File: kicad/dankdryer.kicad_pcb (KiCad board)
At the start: 2 copper layers, 100 x 75 mm, 53 parts, among them J10 HeaderX4, J13 barreljack, J2 to microboard, J3 to baseboard, J4 ScrewX2, J5 ScrewX4, J6 LCD, J7 HeaderX4, J8 ScrewX2, J9 UART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

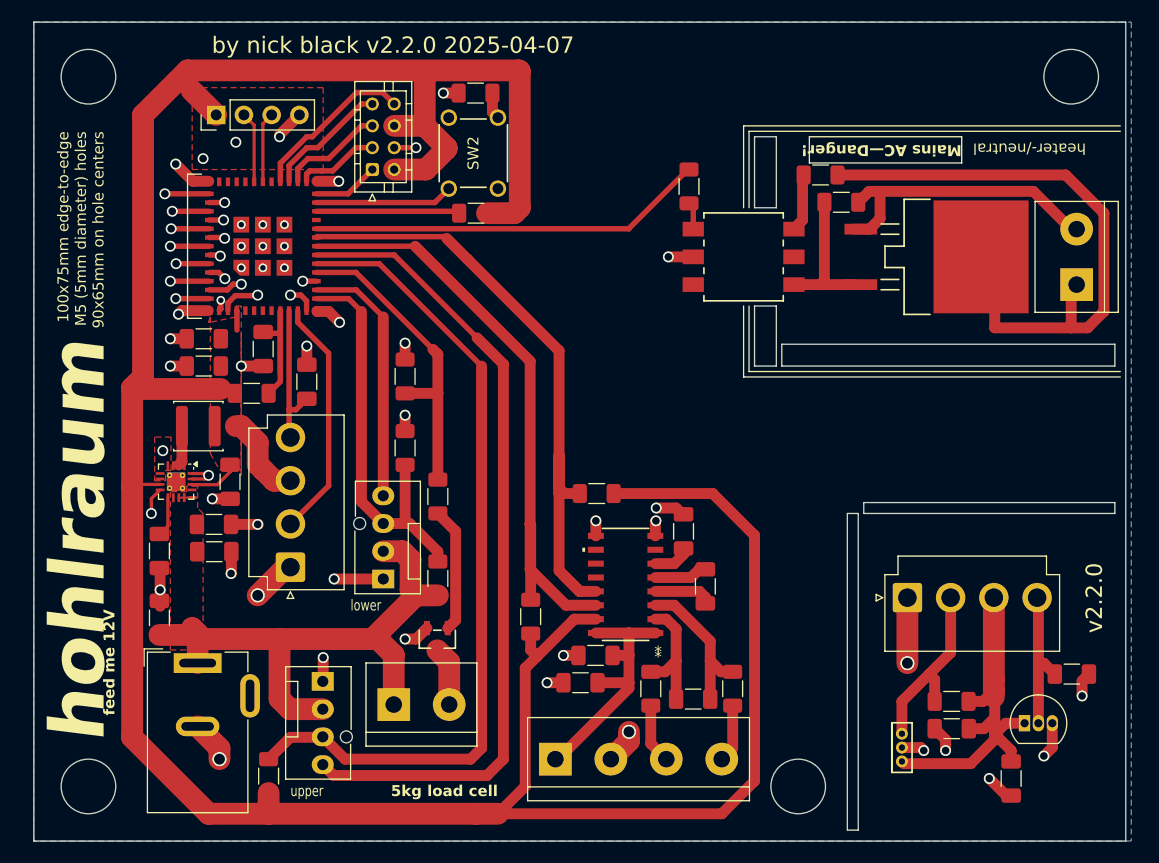
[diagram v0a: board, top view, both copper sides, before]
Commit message: [pcb] eliminate voltage divider before ltach closes #112
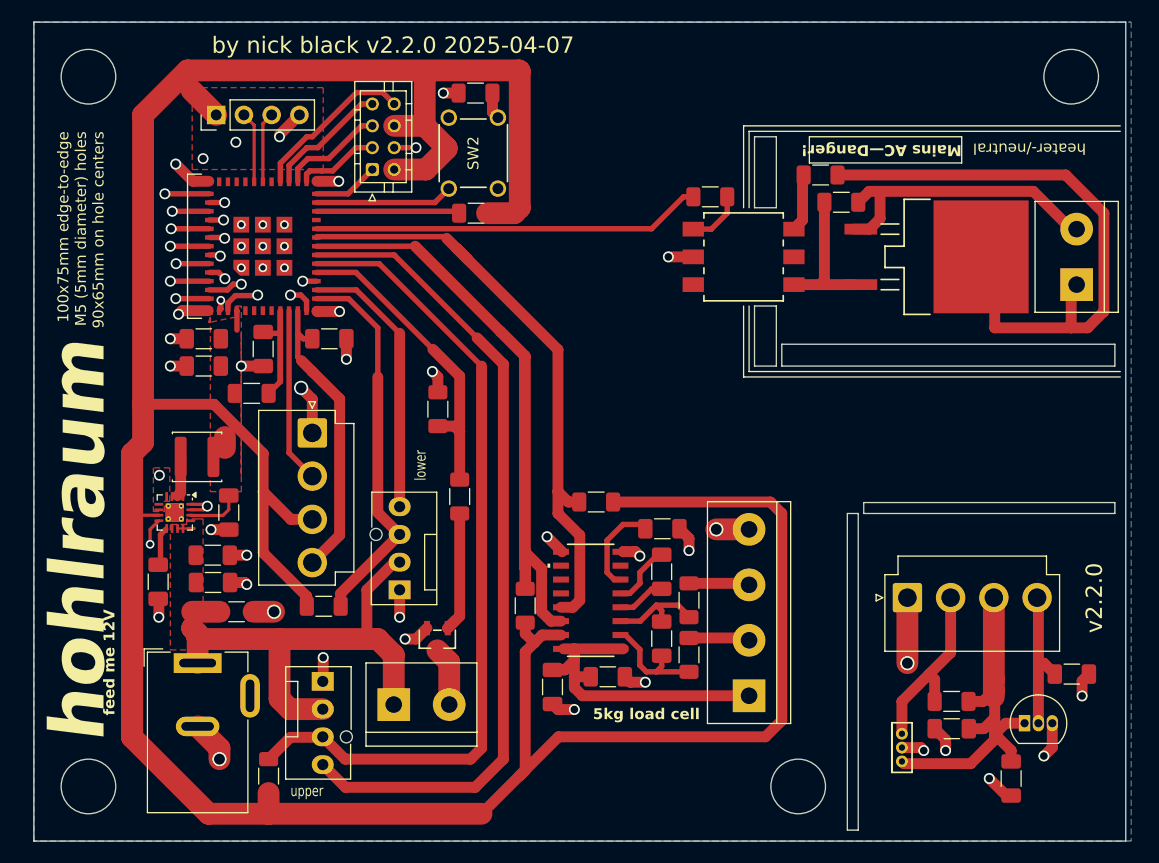
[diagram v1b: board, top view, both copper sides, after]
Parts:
- removed R18: 2.2k, Resistor_SMD:R_1206_3216Metric_Pad1.30x1.75mm_HandSolder
- R5: value 6.8k -> 680
- moved J5 18.7 mm to (115.5, 111.7), turned to 90 degrees
- moved J2 12.5 mm to (75.5, 87.6), turned to -90 degrees
- moved R5 10.8 mm to (76.5, 103.5), turned to 0 degrees
- moved R11 9.03 mm to (110.0, 103.0), turned to -90 degrees
- moved C14 7.08 mm to (68.6, 104.0), turned to 0 degrees
- moved C9 6.24 mm to (107.5, 106.5), turned to 90 degrees
- moved R10 4.68 mm to (110.0, 108.0), turned to -90 degrees
- moved C20 4.44 mm to (77.1, 79.0), turned to 0 degrees
- moved R7 4.24 mm to (87.0, 85.5)
- moved C11 4.22 mm to (107.5, 100.3)
- moved U3 3.51 mm to (101.0, 103.0)
- moved C21 2.82 mm to (67.9, 94.9)
- moved C2 2.82 mm to (66.4, 101.3)
- moved C1 2.82 mm to (66.4, 98.8)
- moved C7 2.82 mm to (61.4, 101.3)
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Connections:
- J5 pad 2: GND -> A-
- J5 pad 3: A- -> A+
- J5 pad 4: A+ -> GND
- R5 pad 1: +12V -> +3.3V
- U6 pad 10: /Hall -> /Therm
- U6 pad 9: /Therm -> /Hall
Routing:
- net +3.3V: track 281.1 -> 319.5 mm
- net /SDA: track 57.3 -> 77.4 mm
- net /Therm: track 13.5 -> 28.6 mm
- net +12V: track 56.3 -> 49.6 mm
- net /Hall: track 22.2 -> 16.0 mm
- net /SCL: track 64.5 -> 58.7 mm
- net Net-(U3-VIN1P): track 14.2 -> 9.00 mm
- net E+: track 24.1 -> 29.2 mm
- net Net-(U3-VBG): track 3.48 -> 8.14 mm
- net Net-(OC1-A): track 2.03 -> 5.21 mm
- net GND: track 134.4 -> 132.4 mm
- net /LTach: track 37.2 -> 35.3 mm
- net Net-(U3-VIN1N): track 11.4 -> 9.75 mm
- net /LPWM: track 23.5 -> 25.2 mm
- net /UPWM: track 75.0 -> 75.9 mm
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
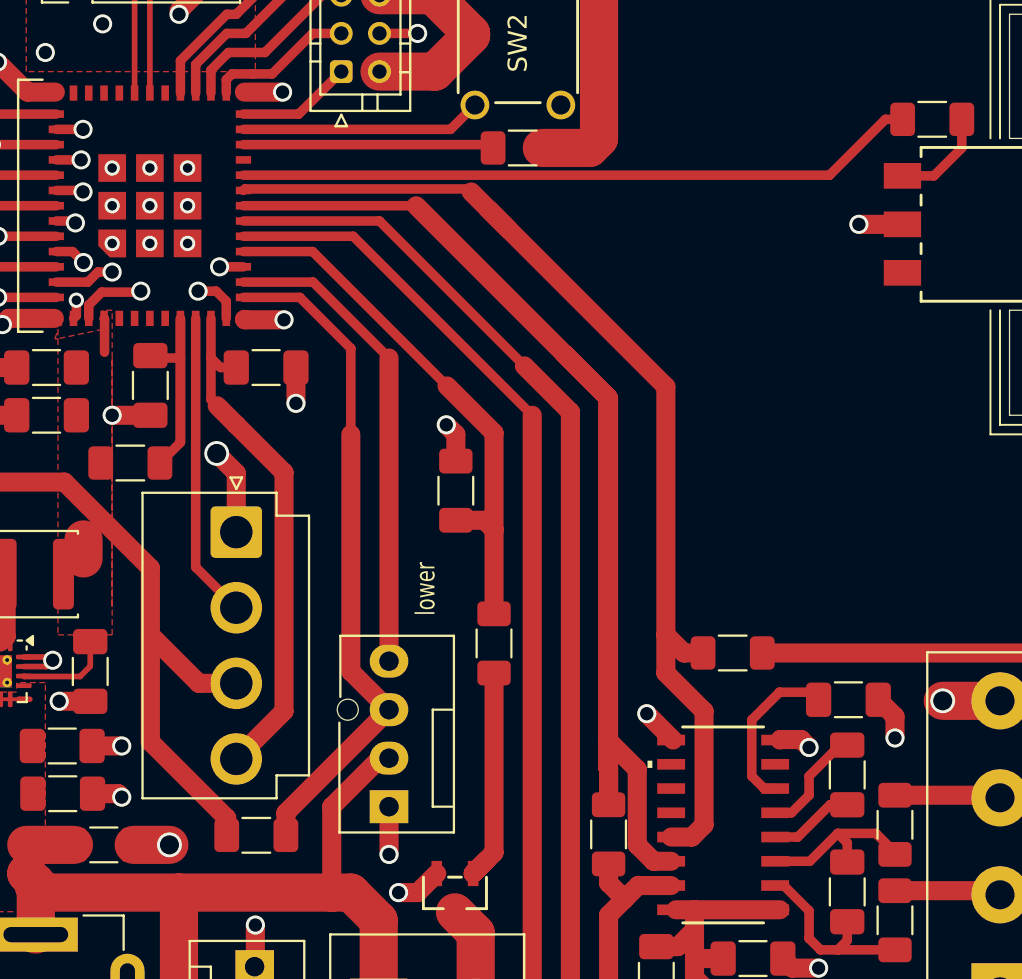
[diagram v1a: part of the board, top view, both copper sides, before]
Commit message: [pcb] reorient load cell hookup
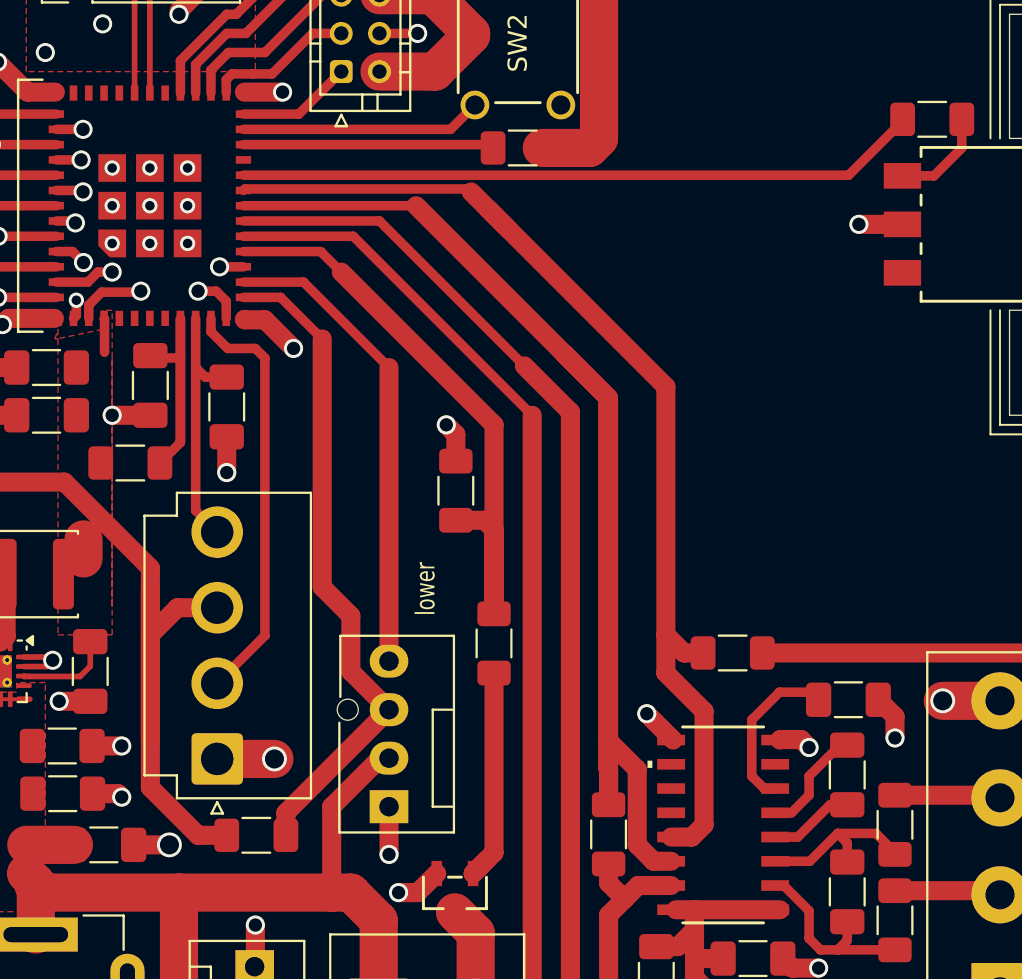
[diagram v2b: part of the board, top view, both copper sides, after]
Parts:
- moved J2 11.9 mm to (74.5, 99.5), turned to 90 degrees
- moved C20 2.92 mm to (75.0, 81.1), turned to -90 degrees
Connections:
- U6 pad 10: /Therm -> /Hall
- U6 pad 9: /Hall -> /Therm
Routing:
- net /Therm: track 28.6 -> 13.5 mm
- net /Motor: track 28.7 -> 38.5 mm
- net +3.3V: track 319.5 -> 327.0 mm
- net /Hall: track 16.0 -> 22.2 mm
- net /LTach: track 35.3 -> 34.7 mm

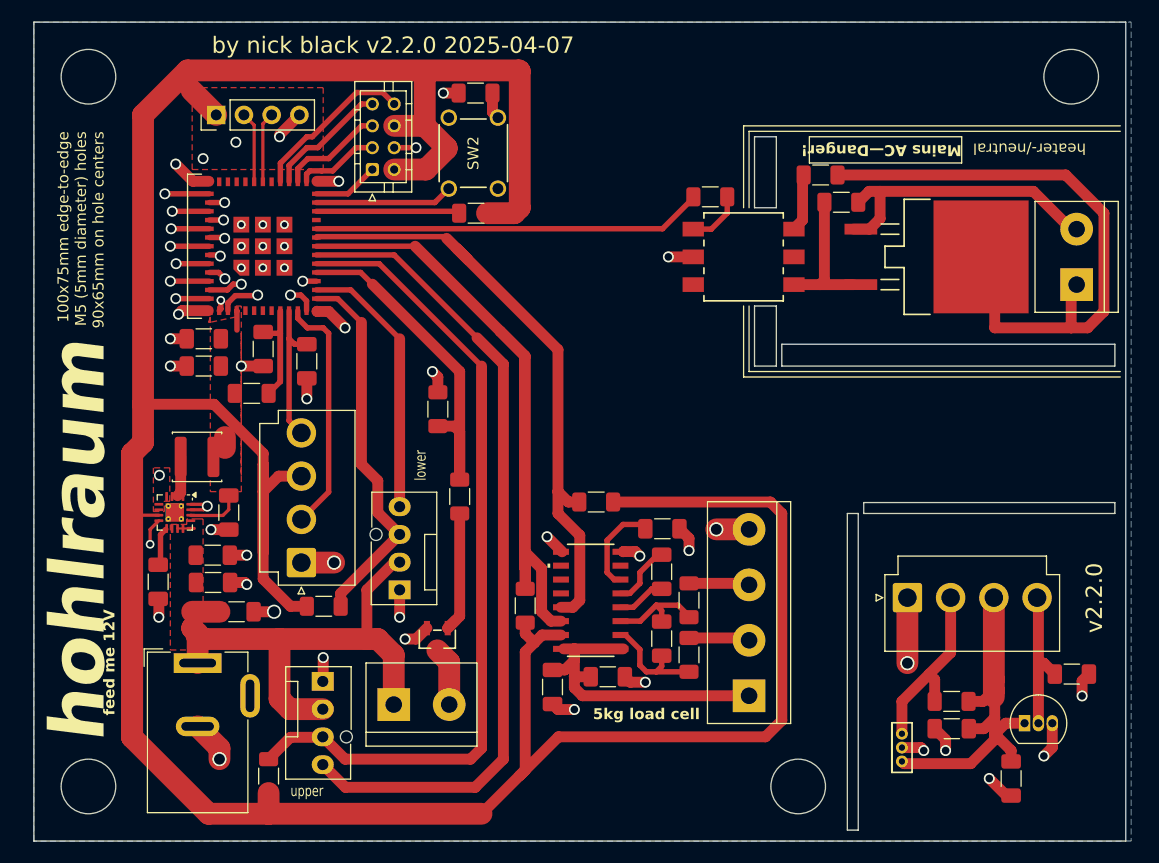
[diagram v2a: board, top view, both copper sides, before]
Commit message: [pcb] label load cell hookups
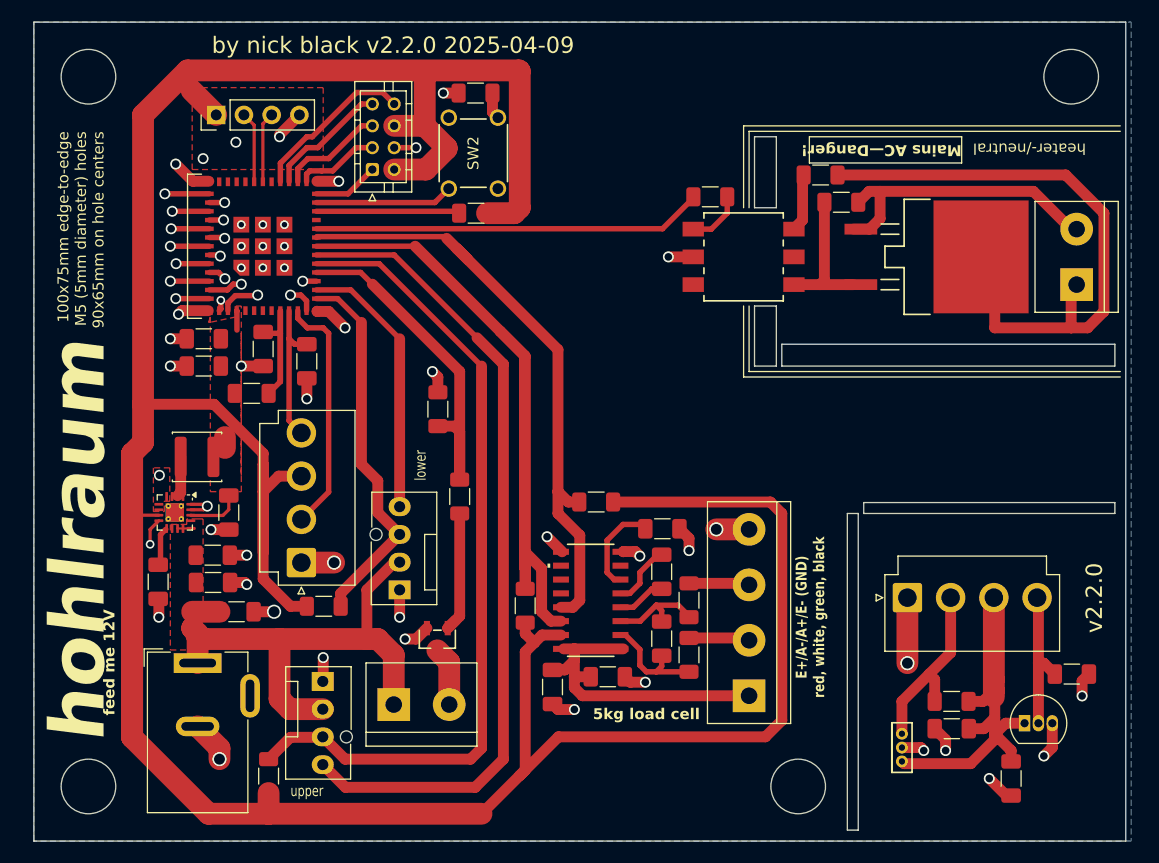
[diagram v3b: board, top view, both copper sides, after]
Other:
- board text added: "E+/A-/A+/E- (GND) red, white, green, black"
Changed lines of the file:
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@@
 	(title_block
 		(title "hohlraum")
-		(date "2025-04-07")
+		(date "2025-04-09")
 		(rev "v2.2.0")
 		(company "dirty south supercomputing")
@@
 		)
 	)
+	(gr_text "E+/A-/A+/E- (GND)\nred, white, green, black"
+		(at 122.5 104.5 90)
+		(layer "F.SilkS")
+		(effects
+			(font
+				(size 1 0.8)
+				(thickness 0.15)
+				(bold yes)
+			)
+			(justify bottom)
+		)
+	)

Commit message: kicad/scad v2.2.2
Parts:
- moved Q1 8.64 mm to (138.0, 119.0), turned to 180 degrees
- moved R8 5.50 mm to (95.0, 109.0)
- moved C8 3.50 mm to (104.1, 96.4), turned to 180 degrees
- moved C11 3.15 mm to (109.0, 97.6)
- moved C19 3.12 mm to (142.1, 117.5), turned to 180 degrees
- moved C12 2.26 mm to (104.6, 111.0)
- moved C5 2.00 mm to (99.5, 111.0)
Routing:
- net /SDA: track 77.4 -> 54.3 mm
- net +3.3Vmicro: track 35.9 -> 28.9 mm
- net /Microboard/HallMicro: track 17.0 -> 22.2 mm
- net GND: track 131.9 -> 127.8 mm
- net Net-(U3-VIN2P): track 5.46 -> 9.23 mm
- net Net-(U3-VIN2N): track 4.48 -> 6.97 mm
- net E+: track 29.2 -> 27.3 mm
- net Net-(U3-VBG): track 8.14 -> 6.88 mm
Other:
- board text added: "Keep througholes 5mm x 5mm apart."
- board text removed: "5kg load cell"

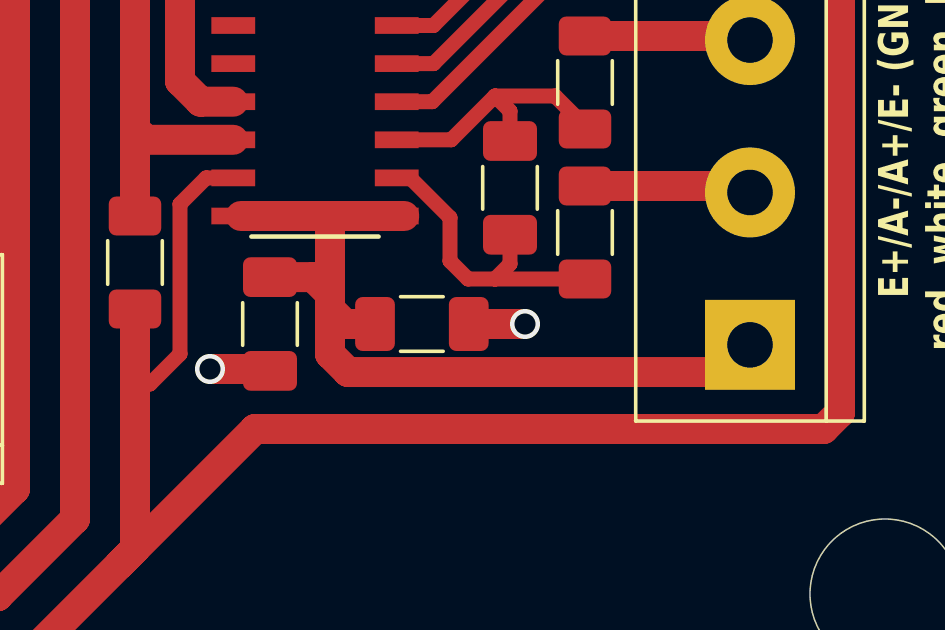
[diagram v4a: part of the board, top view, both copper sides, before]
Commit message: move NAU7802 capacitors
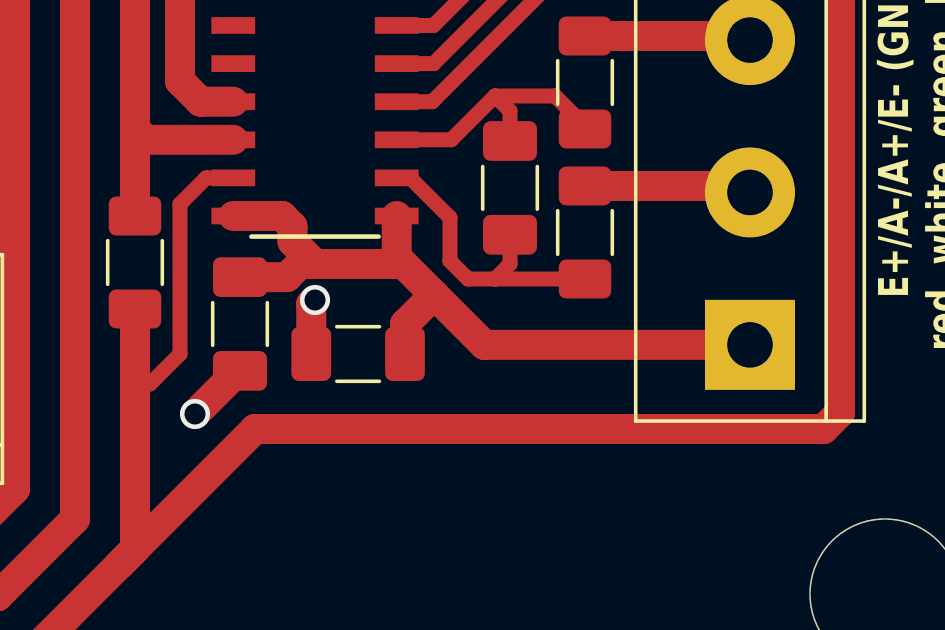
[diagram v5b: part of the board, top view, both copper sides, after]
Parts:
- moved C12 6.06 mm to (98.5, 111.0), turned to -90 degrees
- moved C5 3.10 mm to (102.4, 112.0), turned to 180 degrees
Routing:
- net E+: track 27.3 -> 26.0 mm
